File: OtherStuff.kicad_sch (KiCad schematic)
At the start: 35 parts, among them IC601 MMS9013-L-TP, IC602 MMS9013-L-TP, J601 USB_B_Micro, X601 XTAL_4_PINS, X602 XTAL_2_PINS

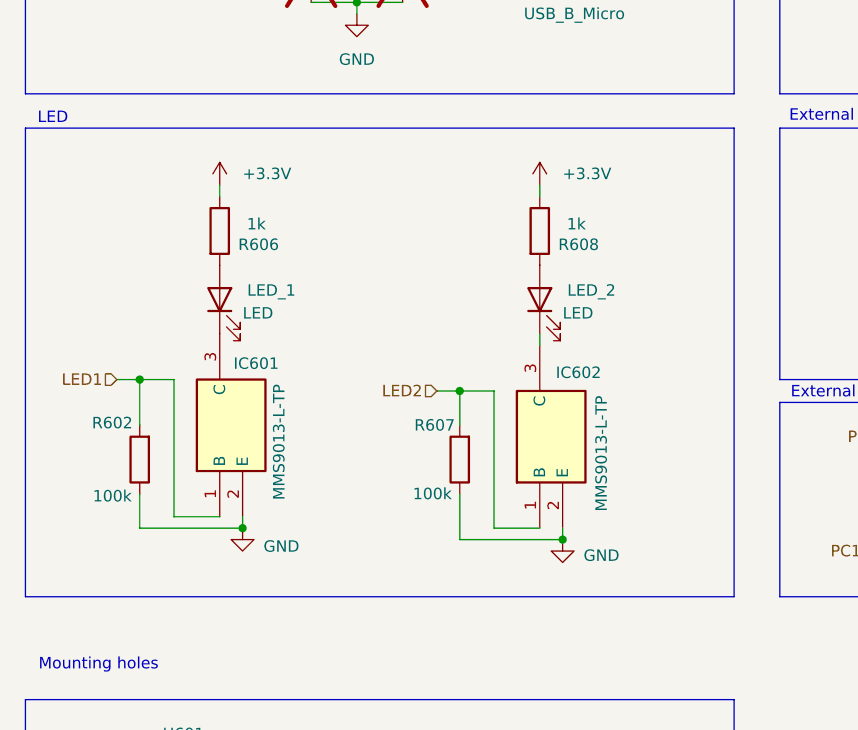
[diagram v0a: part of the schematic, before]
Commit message: Add SamacSys & CAPPRD library; update KiCad
Add a new SamacSys parts library and a complete CAPPRD500 footprint/package set (870585375004) with multi-EDA exports and 3D STEP models. Also add sym-lib-table and SamacSys parts entries, and update KiCad project files (schematics, PCB, project file and generated PDFs) to reference the new parts and footprints.
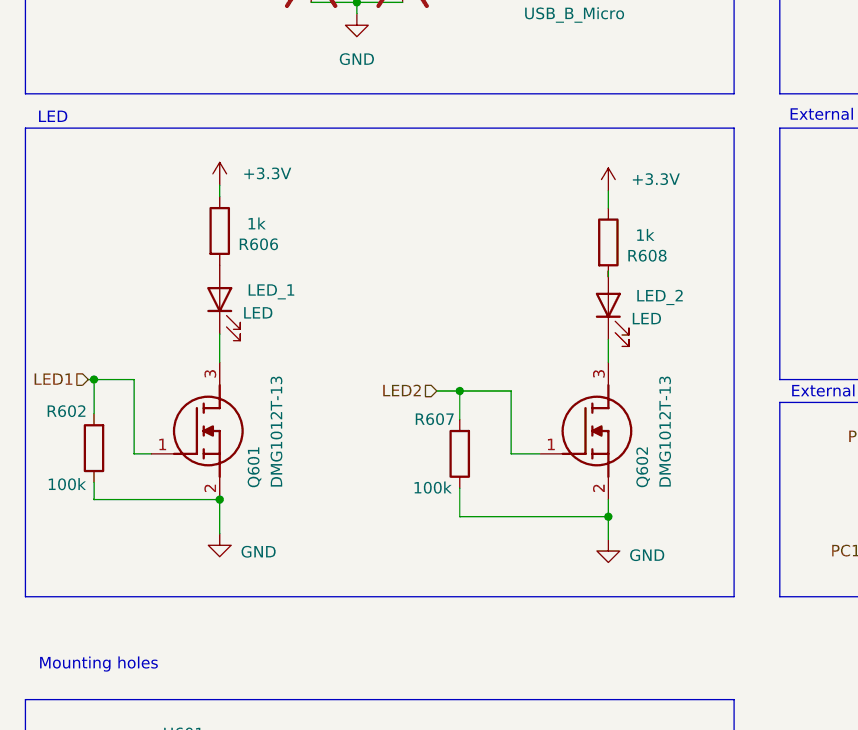
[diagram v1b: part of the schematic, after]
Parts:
- removed IC601, IC602: MMS9013-L-TP, MMS-9013:SOT95P237X125-3N, symbol MMS-9013:MMS9013-L-TP
- added Q601, Q602: DMG1012T-13, DMG1012T:SOT50P160X90-3N, symbol MOSFET_Nchannel_DMG1012T-13:DMG1012T-13
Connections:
- net GND: now also Q601.2 (S), Q602.2 (S)
- net LED1: now also Q601.1 (G)
- net LED2: now also Q602.1 (G)
- net at LED_1.1 (K): now also Q601.3 (D)
- net at LED_2.1 (K): now also Q602.3 (D)
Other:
- moved on the sheet: LED_2, R602, R607, R608
